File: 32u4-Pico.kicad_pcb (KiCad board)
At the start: 2 copper layers, 21.1 x 51.3 mm, 24 parts, among them J3 2.54mm header 01x20, J4 2.54mm header 01x20, U1 ATmega32U4-MU, U2 3.3VO SOT-23, X1 8Mhz 3225

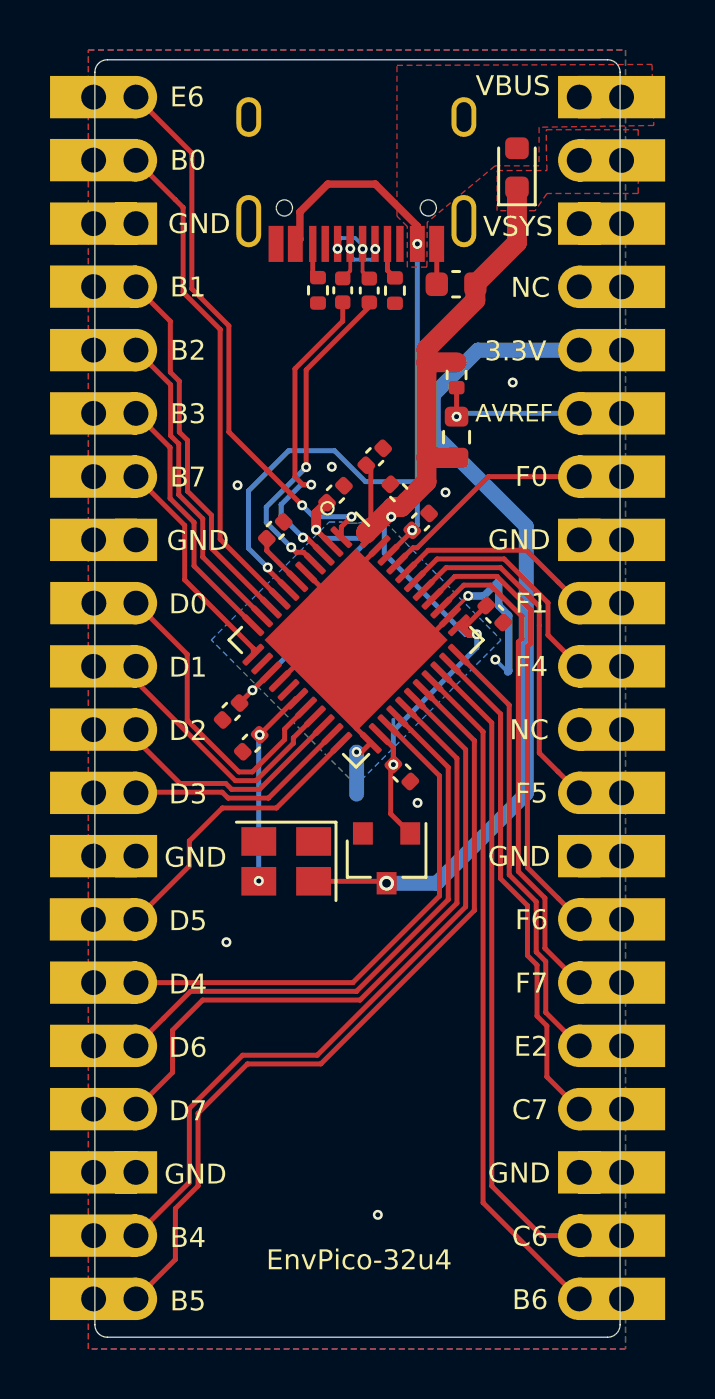
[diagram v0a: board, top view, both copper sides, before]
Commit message: implemented Rest pin in place of RUN and added a reset button + a couple other bits
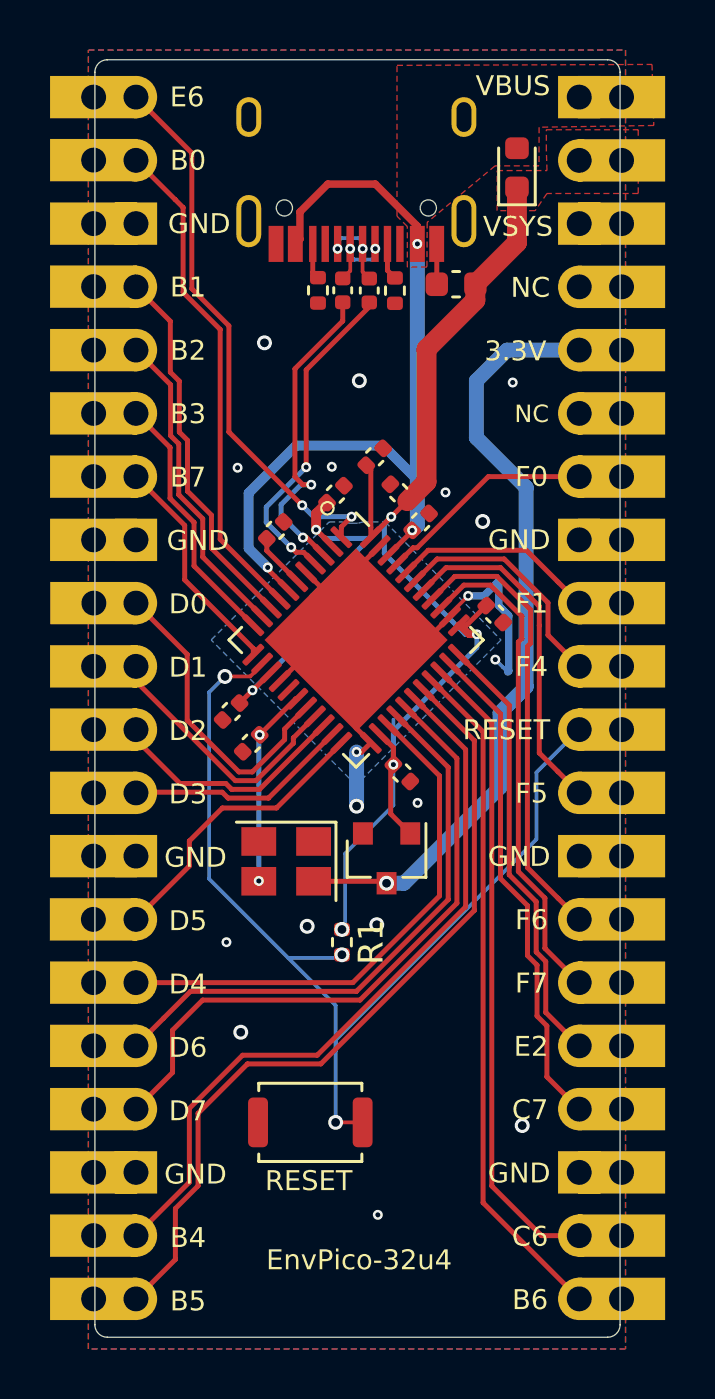
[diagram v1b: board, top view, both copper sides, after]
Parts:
- removed R10: 1Ohm 0402, Resistor_SMD:R_0402_1005Metric
- removed R9: 200ohm 0603, Resistor_SMD:R_0603_1608Metric
- added R1: 10K 0402, Resistor_SMD:R_0402_1005Metric, F.Cu at (103.0, 92.7)
- added RSW1: SKRK, Button_Switch_SMD:SW_Push_SPST_NO_Alps_SKRK, F.Cu at (101.8, 99.9)
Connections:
- U1 pad 13: (no net) -> /RUN
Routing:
- net /RUN: track 0.00 -> 42.3 mm, vias 0 -> 3
- net /ADC_VREF: track 6.14 -> 0.00 mm, vias 1 -> 0
- net +3V3: track 34.2 -> 31.3 mm
- net VSYS: track 62.3 -> 65.0 mm, vias 5 -> 6
- net VBUS: track 33.5 -> 35.7 mm
- net GND: track 31.2 -> 31.7 mm, vias 10 -> 18
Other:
- board text added: "RESET"
- board text removed: "AVREF"

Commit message: more via fixes and all.
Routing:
- net USB_D+: track 3.21 -> 5.47 mm
- net USB_D-: track 3.01 -> 4.87 mm

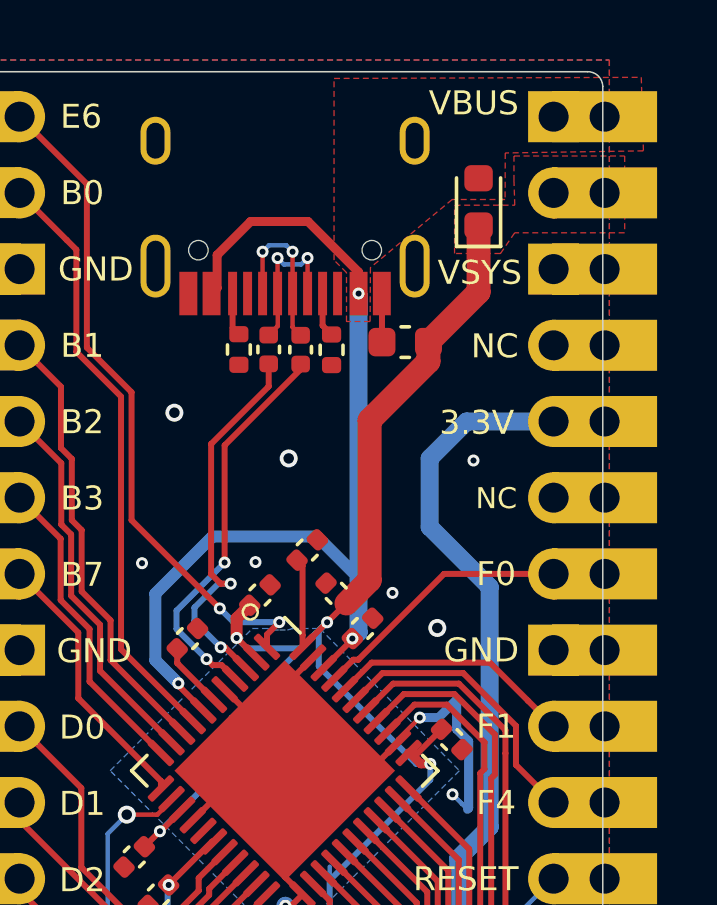
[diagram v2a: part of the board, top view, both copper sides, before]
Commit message: Added keepout zones near the pin holes and corrected all errors as per DRC.
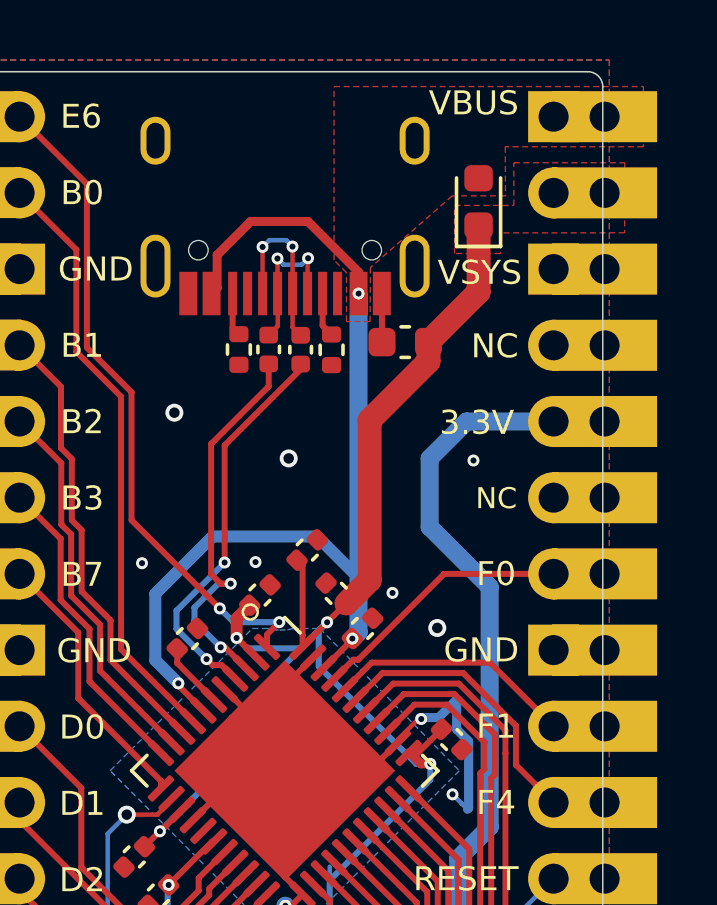
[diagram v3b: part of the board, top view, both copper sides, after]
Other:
- rule trace_min: 0.15 -> 0.2

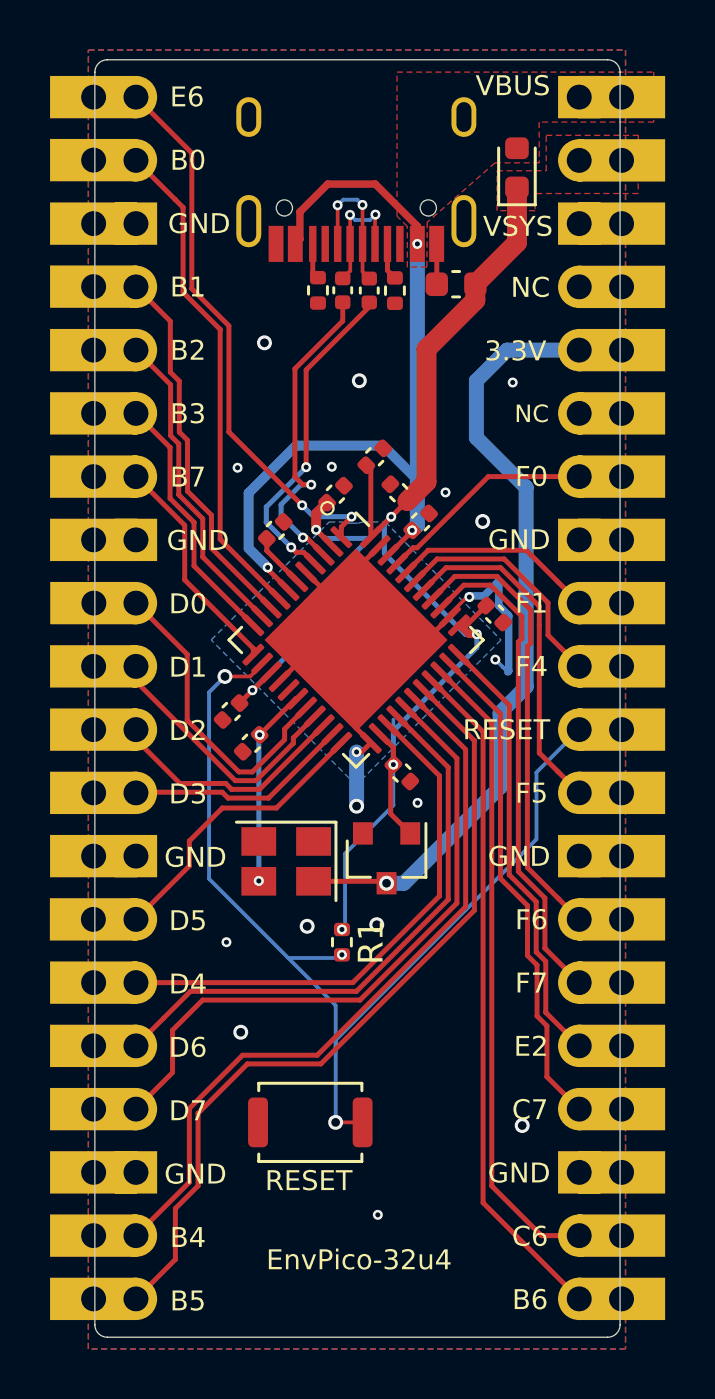
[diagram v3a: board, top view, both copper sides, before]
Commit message: swapped oscillator for crystal because easier to get a hold of as of right now. (and a bit of tidying up)
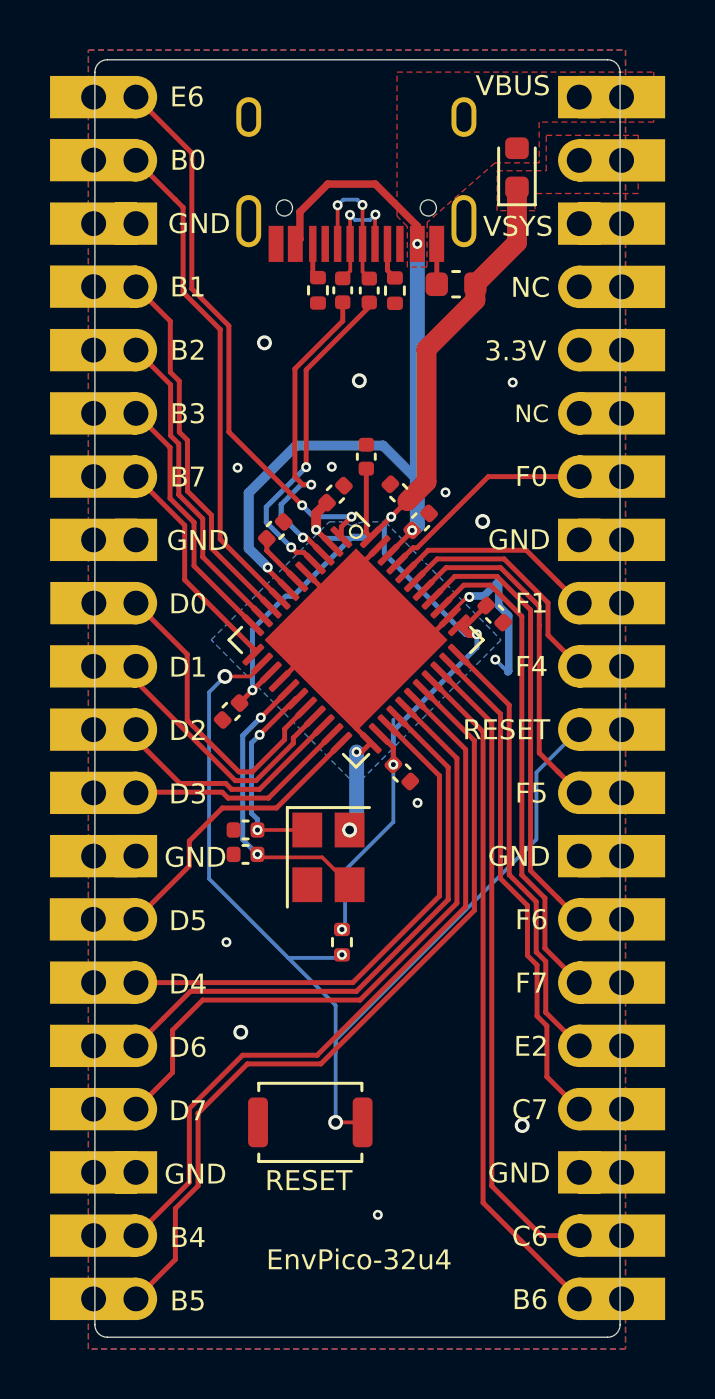
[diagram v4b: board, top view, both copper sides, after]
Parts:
- removed U2: 3.3VO SOT-23, Package_TO_SOT_SMD:SOT-23
- removed X1: 8Mhz 3225, Crystal:Crystal_SMD_SeikoEpson_TSX3225-4Pin_3.2x2.5mm
- added C7: 22pF 0402, Capacitor_SMD:C_0402_1005Metric, F.Cu at (99.2, 89.1)
- added Y1: 8MHz 3225_4p crystal, Crystal:Crystal_SMD_3225-4Pin_3.2x2.5mm, F.Cu at (102.5, 89.3)
- C2: value 15pf 0402 -> 22pF 0402
- R3, R4: value 27Ohms 0402 Resistor -> 22Ohm 0402 Resistor
- moved C2 3.49 mm to (99.2, 88.2), turned to 0 degrees
- moved C10 0.34 mm to (104.0, 73.2), turned to 90 degrees
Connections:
- net /XIN renamed XTAL1
- U1 pad 16: (no net) -> XTAL2
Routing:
- net +3V3: track 31.3 -> 0.00 mm, vias 1 -> 0
- net XTAL2: track 0.00 -> 11.8 mm, vias 0 -> 2
- net VSYS: track 65.0 -> 62.5 mm
- net GND: track 31.7 -> 32.8 mm, vias 18 -> 16
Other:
- rule trace_min: 0.2 -> 0.15

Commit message: small adjustment fix for the vbus/vsys diode.
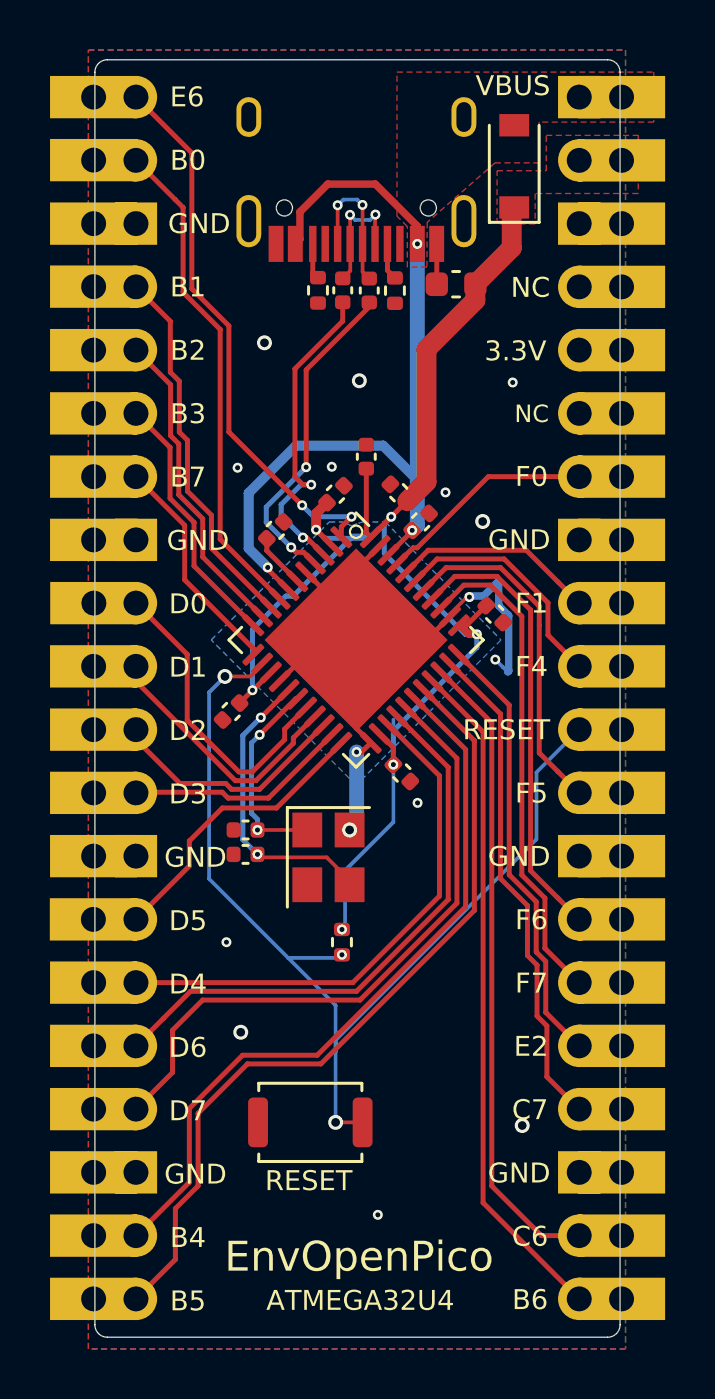
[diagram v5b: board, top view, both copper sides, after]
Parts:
- D1: value Schottky 0603 -> 1n40002; footprint Diode_SMD:D_0603_1608Metric -> Diode_SMD:D_SOD-123
- moved D1 0.13 mm to (109.9, 61.5)
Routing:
- net VSYS: track 62.5 -> 61.8 mm
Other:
- board text added: "ATMEGA32U4"
- board text added: "EnvOpenPico"
- board text removed: "EnvPico-32u4"
- board text removed: "There is no treasure here"
- board text removed: "VSYS"

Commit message: added ISP header on board and routed traces for it.
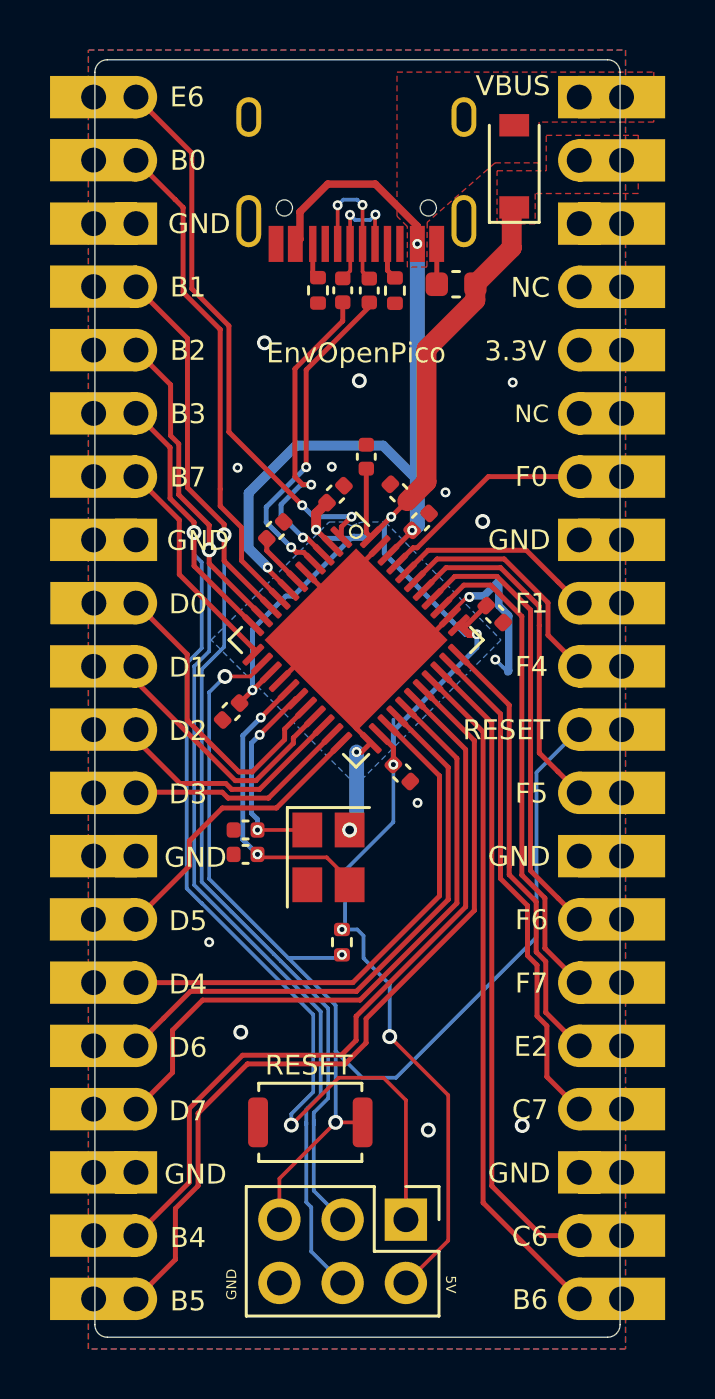
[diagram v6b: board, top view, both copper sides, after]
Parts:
- added ISP1: AVR-ISP-6, Connector_PinHeader_2.54mm:PinHeader_2x03_P2.54mm_Vertical, F.Cu at (105.6, 103.8)
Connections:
- net /GPIO2 renamed GPIO2-SCK
- net /GPIO3 renamed GPIO3-mosi
- net /GPIO4 renamed GPIO4-miso
- net /RUN renamed RUN-RESET
- e1 pad 3: (no net) -> Net-(e1-Pad3)
- e1 pad 9: (no net) -> Net-(e1-Pad9)
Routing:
- net GPIO4-miso: track 10.5 -> 47.7 mm, vias 0 -> 2
- net GPIO3-mosi: track 12.8 -> 45.5 mm, vias 0 -> 1
- net GPIO2-SCK: track 15.1 -> 46.0 mm, vias 0 -> 1
- net VSYS: track 61.8 -> 78.8 mm, vias 6 -> 7
- net RUN-RESET: track 42.3 -> 50.0 mm
- net /GPIO15: track 32.7 -> 33.2 mm
- net /GPIO14: track 29.6 -> 30.2 mm
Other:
- board text added: "5V"
- board text removed: "ATMEGA32U4"

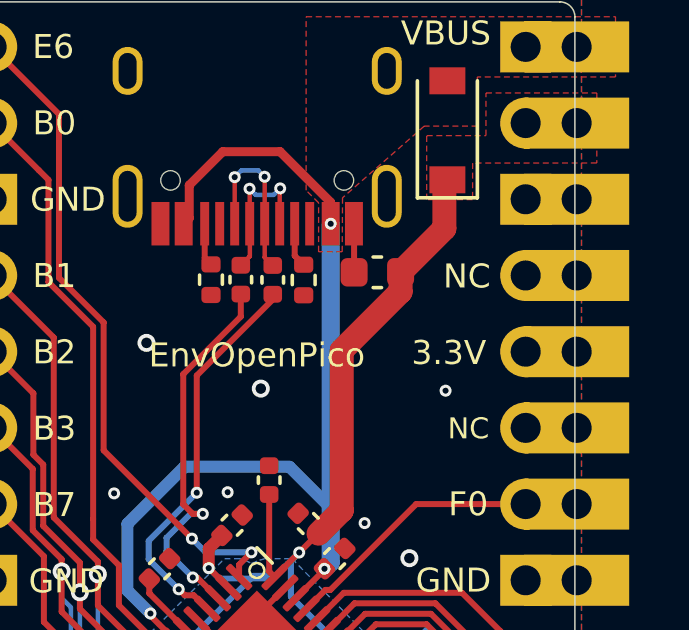
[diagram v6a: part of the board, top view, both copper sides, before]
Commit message: fixed a few silkscreen bits, i.e 3.3V to NC
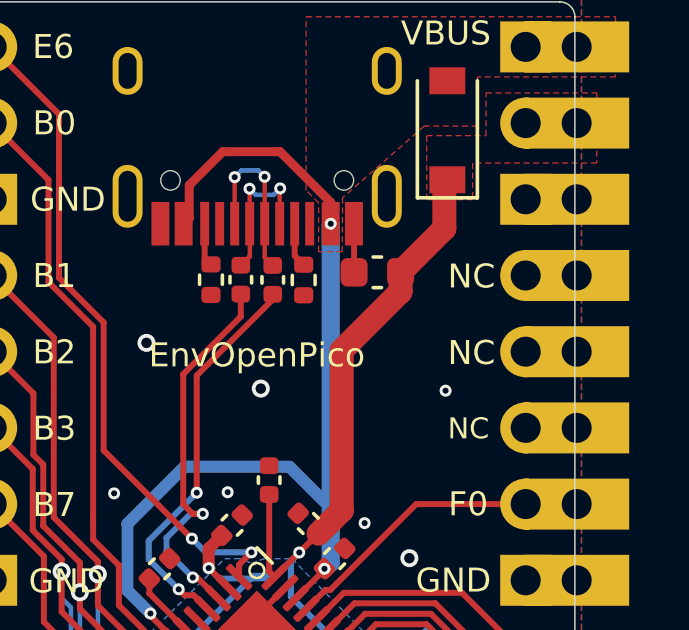
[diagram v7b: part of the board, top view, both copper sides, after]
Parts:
- moved G*** 20.8 mm to (103.7, 80.5)
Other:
- board text removed: "3.3V"

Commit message: Generated updated gerber and stuff
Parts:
- moved G*** 12.4 mm to (103.7, 68.1)
- moved ISP1 0.60 mm to (106.2, 103.8)
- renumbered e1 to USB1
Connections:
- USB1 pad 3: Net-(e1-Pad3) -> (no net)
- USB1 pad 9: Net-(e1-Pad9) -> (no net)
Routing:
- net GND: track 32.8 -> 35.4 mm, vias 16 -> 18
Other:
- board size 21.1 x 51.3 mm -> 21.3 x 51.3 mm
- board text added: "EnvOpenPico ATmega32U4"
- board text removed: "EnvOpenPico"
